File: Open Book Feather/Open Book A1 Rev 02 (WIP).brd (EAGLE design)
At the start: 77.5 x 112.3 mm, 124 parts, among them J1 SJ-43514-SMT, J2 10118193-0001LF, Q1 DMG341, Q2 IRLML0100, SW1 SPDT_SWITCH, U1 AP2112-3.3, U2 MCP73831T-2ACI/OT, U3 ATSAMD51J64-TQFP(10X10), U4 GD25Q16C (or GD25Q32C), U5 74AC165D, U6 GD25Q16C (or GD25Q32C), U7 23K256-I/SN, U8 MAX4466EXK+T, X1 JSTPH, X2 2x5 0.05" SWD

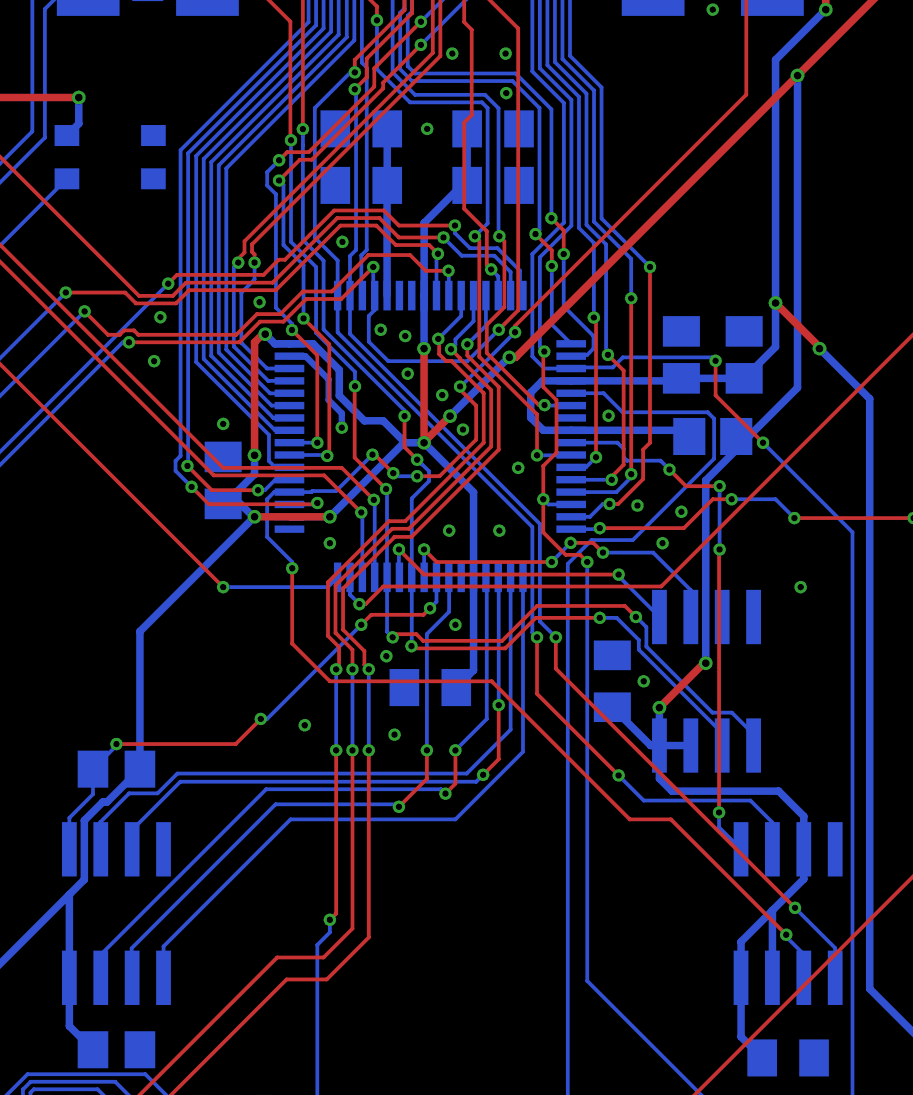
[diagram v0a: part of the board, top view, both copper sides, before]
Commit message: tweak documentation of QSPI flash
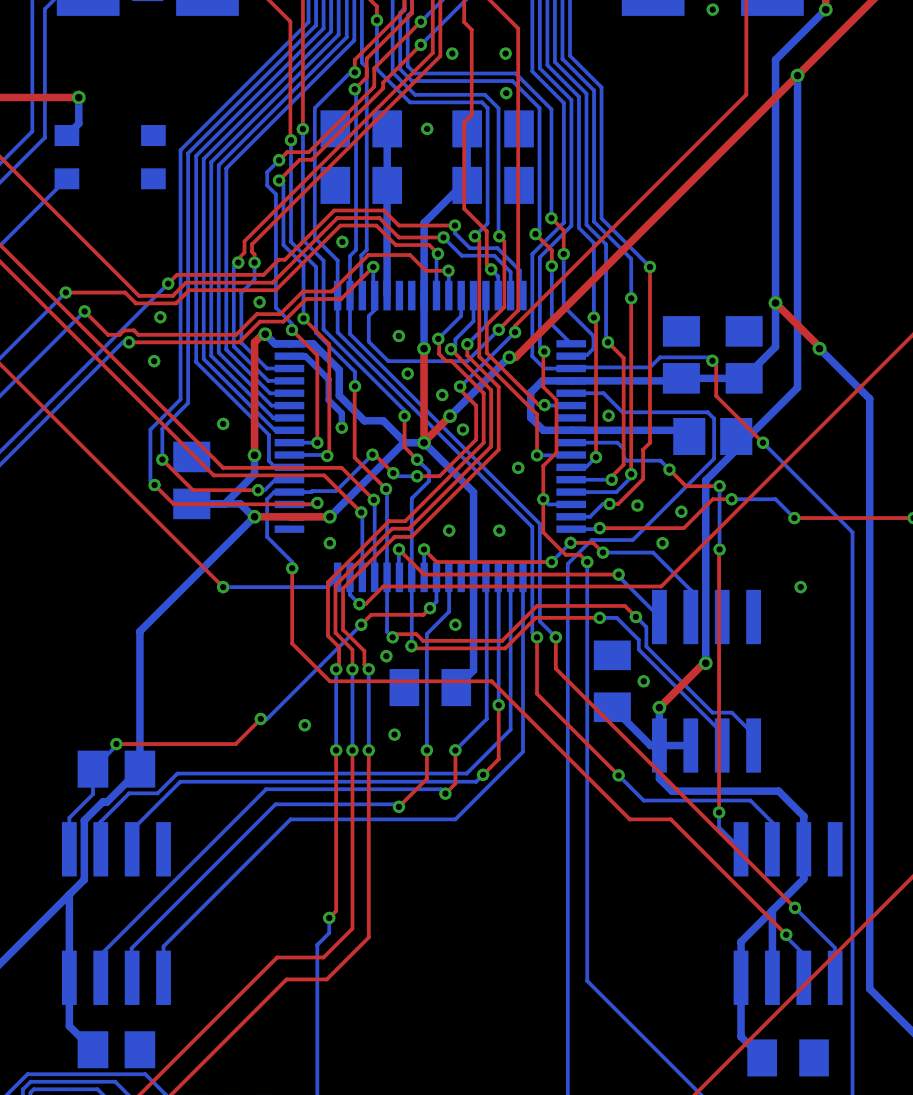
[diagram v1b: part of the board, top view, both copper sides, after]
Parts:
- moved C7 1.27 mm to (29.2, 48.3)
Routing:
- net +3V3: track 531.7 -> 534.3 mm
- net D5: track 41.3 -> 43.0 mm
- net D6: track 41.0 -> 42.3 mm
- net GND: vias 50 -> 49
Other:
- board text added: "U4 is another GD25Q16C Flash chip. It's the CIRCUITPY drive that shows up when you plug it in! It's on a dedicated QSPI bus (D35-D40/PA08-PA11, PB10, PB11). R9 pulls U4's CS high; the microcontroller can drive it low (active) via QSPI_CS (D36)."
- board text removed: "U4 is another GD25Q16C Flash chip on a dedicated QSPI bus (D35-D40/PA08-PA11 & PB10- PB11). It's the CIRCUITPY drive that shows up when you plug it in! R9 pulls U4's CS high; the microcontroller can drive it low (active) via QSPI_CS (D36)."

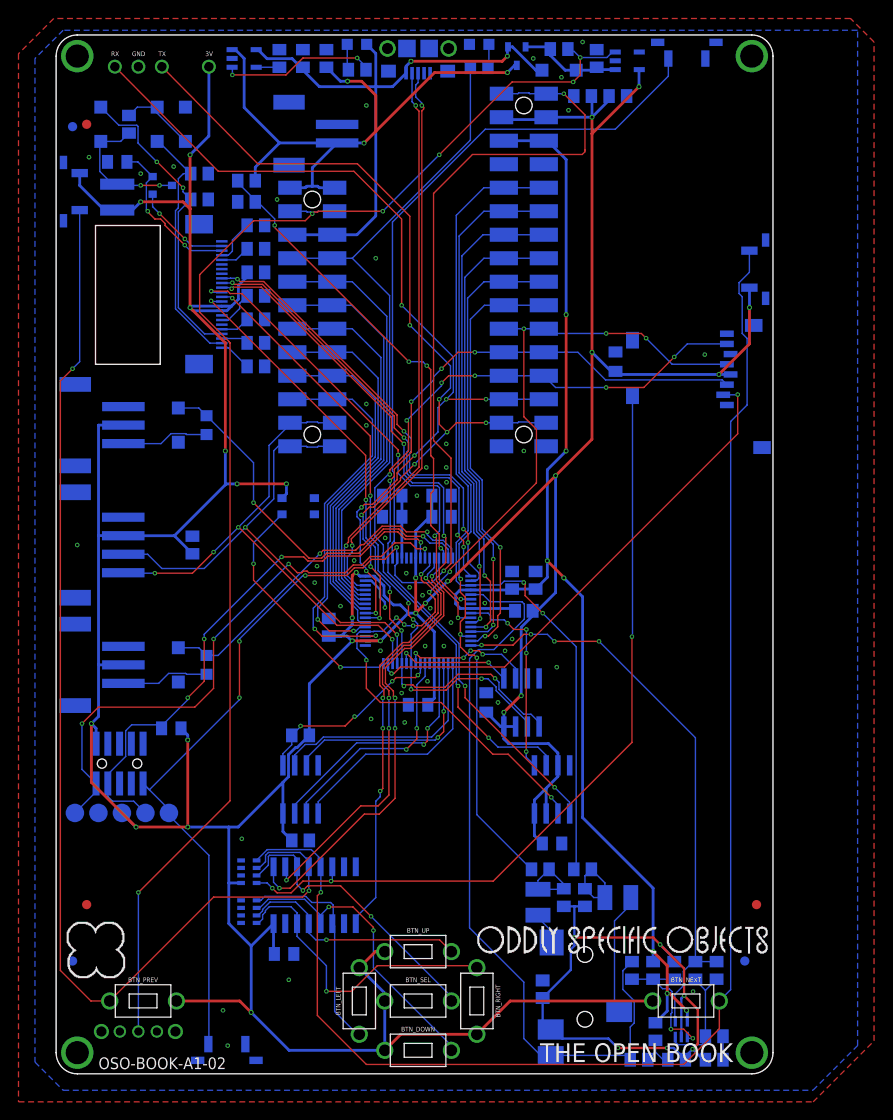
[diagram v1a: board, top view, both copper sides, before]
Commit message: more silkscreen tweaks
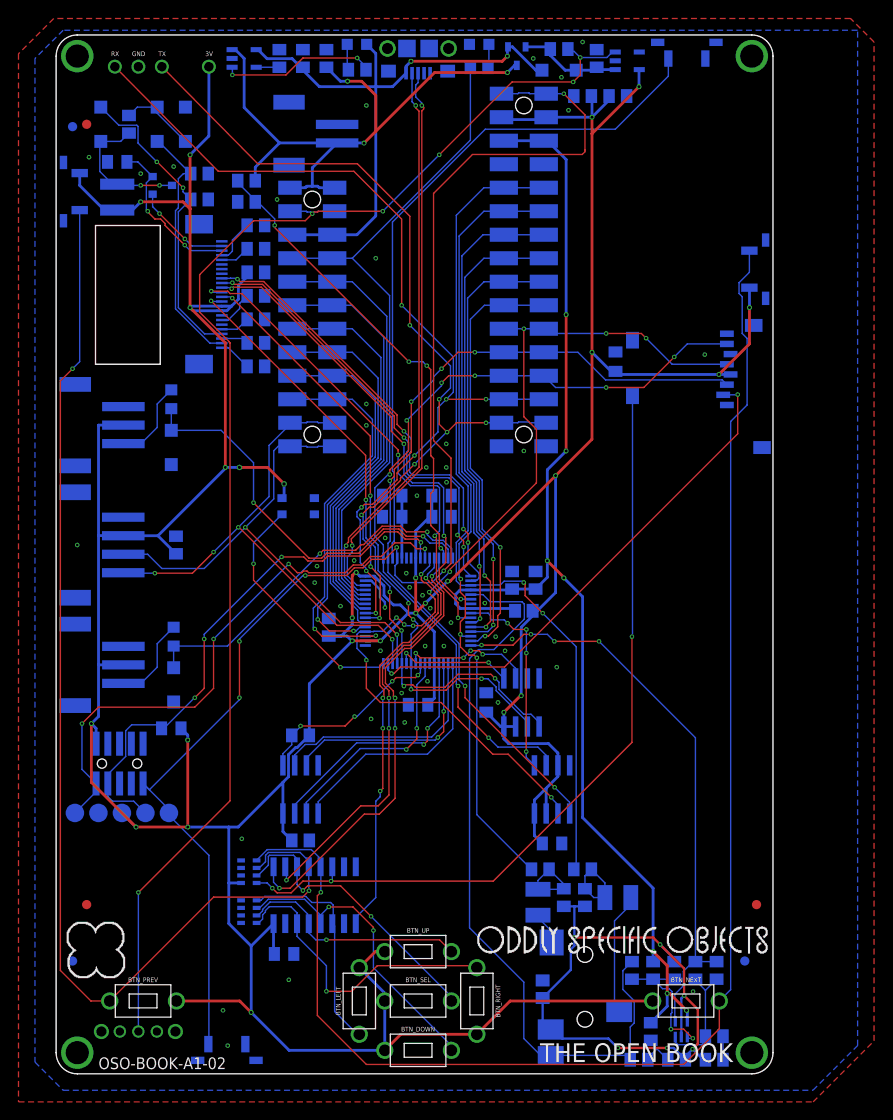
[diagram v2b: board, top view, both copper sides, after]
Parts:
- moved R18 4.72 mm to (12.2, 72.9), turned to 270 degrees
- moved R17 4.68 mm to (12.4, 47.2), turned to 270 degrees
- moved D6 2.53 mm to (12.2, 67.7)
- moved D5 2.22 mm to (12.4, 42.0)
- moved C27 1.78 mm to (12.7, 57.1)
- moved R23 0.51 mm to (64.0, 4.57)
- moved U$45 0.13 mm to (38.5, 94.2)
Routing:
- net D3_A9: track 41.6 -> 43.7 mm
- net D2_A8: track 37.9 -> 40.0 mm
- net N$65: track 4.12 -> 4.96 mm
- net +3V3: track 534.3 -> 533.6 mm
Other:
- board text added: "A8"
- board text added: "A9"
- board text added: "The Open Book by Joey Castillo @josecastillo. Based in large part on @Adafruit's awesome open source designs! OSO logo & lazer bear by Joseph Devens, @DoctorDevens. Thanks to Tom F, Josh L, Brent R & many others. Made with . in Brooklyn & Texas."
- board text added: "The center port provides an I²C interface. The other two ports provide access to pins A8 and A9 (PB03 & PB02, respectively) via current limiting resistors R17 & R18. D5 & D6 are 3.6V zener diodes to protect pins from overvoltage: they shunt excess power to ground when voltage exceeds their breakdown point."
- board text removed: "A1"
- board text removed: "A2"
- board text removed: "The Open Book by Joey Castillo @josecastillo. Based in large part on @Adafruit's great open source designs. OSO logo & lazer bear by Joseph Devens, @DoctorDevens. Thanks to Tom F, Josh L, Brent R & many others. Made with . in Brooklyn & Texas."
- board text removed: "The center port provides an I2C interface. The other two ports provide access to pins A8 and A9. D5 & D6 + R17 & R18 provide protection and current limiting."

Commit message: renumber passives, update silkscreen
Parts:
- removed C35: 10uF, microbuilder:0805-NO
- removed R26, R27: 100K, resistor array:EXBV8V
- added C13: 1uF, microbuilder:0805-NO
- added R6: 270, microbuilder:0805-NO
- added R7: 100K, microbuilder:0805-NO
- C17: value 1uF -> 1uF/25V
- C23: value 1uF/25V -> 4.7uF/25V
- C24: value 4.7uF/25V -> 10uF; device microbuilder:0805-NO -> microbuilder:0805_10MGAP
- C25: value 10uF -> 1uF
- C26: value 1uF -> 10uF; device microbuilder:0805_10MGAP -> microbuilder:0805-NO
- C27: value 10uF -> 1uF; device microbuilder:0805-NO -> microbuilder:0805_10MGAP
- C29: value 1uF -> 100uF; device microbuilder:0805_10MGAP -> resistor:C1210
- C31: value 100uF -> 0.1µF; device resistor:C1210 -> microbuilder:0805-NO
- C32: value 0.1µF -> 0.01uF
- C33: value 0.01uF -> 100pF
- C34: value 100pF -> 10uF
- R10: value 1M -> 0.47ohm; device microbuilder:0805-NO -> microbuilder:0805_10MGAP
- R11: value 1M -> 100K; device microbuilder:0805-NO -> resistor array:EXBV8V
- R12: device microbuilder:0805-NO -> resistor array:EXBV8V
- R13: device microbuilder:0805-NO -> microbuilder:_0805MP
- R14: value 100K -> 1K; device microbuilder:0805-NO -> microbuilder:_0805MP
- R15: value 100K -> 100
- R16: value 0.47ohm -> 100; device microbuilder:0805_10MGAP -> microbuilder:0805-NO
- R17, R18: value 1K -> 100; device microbuilder:_0805MP -> microbuilder:0805-NO
- R19, R20: value 100 -> 1K
- R21, R22: value 100 -> 1M
- R24: value 1K -> 100K
- R8: value 270 -> 100K
- moved R10 106.1 mm to (6.35, 98.6), turned to 0 degrees
- moved R16 94.2 mm to (56.9, 19.1), turned to 90 degrees
- moved R15 82.8 mm to (56.6, 22.1)
- moved C25 73.3 mm to (24.4, 13.0), turned to 180 degrees
- moved R18 68.5 mm to (54.6, 19.1), turned to 90 degrees
- moved R13 68.0 mm to (12.4, 47.2), turned to 270 degrees
- moved C14 66.6 mm to (21.3, 91.7), turned to 0 degrees
- moved C24 58.5 mm to (60.2, 77.0)
- moved R9 58.0 mm to (20.3, 94.2)
- moved C27 51.9 mm to (53.3, 24.9), turned to 180 degrees
- moved R12 48.7 mm to (20.6, 17.5), turned to 0 degrees
- moved R17 46.9 mm to (52.1, 22.1), turned to 0 degrees
- moved C26 45.7 mm to (12.7, 57.1), turned to 90 degrees
- moved R11 45.0 mm to (20.6, 21.8), turned to 0 degrees
- moved R8 28.0 mm to (20.3, 96.5), turned to 0 degrees
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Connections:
- net +3V3: now also C13.1, C16.2, C24.1, R11.5, R7.1; no longer C14.1, C17.2, C29.1, R26.5, R9.1
- net A0: now also R15.2; no longer R19.2
- net A1: now also R17.2; no longer R21.2
- net A10_MICAMP: now also C33.1, R24.2; no longer C34.1, R12.2
- net A6_VMEAS: now also R8.2, R9.1; no longer R14.1, R15.2
- net A7_MIC: now also C32.1, R19.1; no longer C33.1, R13.1
- net A8_: now also R13.1; no longer R17.1
- net A9_: now also R14.1; no longer R18.1
- net AGND: now also C31.2, C34.2, R16.1, R18.1, R21.1; no longer C32.2, C35.2, R10.1, R20.1, R22.1
- net AUDIO_LEFT: now also C30.2; no longer C31.2
- net AUDIO_RIGHT: now also C29.2; no longer C30.2
- net AVCC: now also R20.2, R22.2; no longer R11.2, R23.2
- net BUTTON0: now also R12.1; no longer R27.1
- net BUTTON1: now also R12.2; no longer R27.2
- net BUTTON2: now also R12.3; no longer R27.3
- net BUTTON3: now also R12.4; no longer R27.4
- net BUTTON4: now also R11.3; no longer R26.3
- net BUTTON5: now also R11.2; no longer R26.2
- net BUTTON6: now also R11.1; no longer R26.1
- net BUTTON7: now also R11.4; no longer R26.4
- net D13: now also R6.1; no longer R8.1
- net D2_A8: now also R13.2; no longer R17.2
- net D3_A9: now also R14.2; no longer R18.2
- net GND: now also C13.2, C14.1, C21.2, C24.2, R10.2, R11.6, R11.7, R11.8, R12.5, R12.6, R12.7, R12.8, R9.2; no longer C14.2, C21.1, C23.2, C29.2, R14.2, R16.2, R26.6, R26.7, R26.8, R27.5, R27.6, R27.7, R27.8
- net N$15: now also C30.1, R17.1, R18.2; no longer C31.1, R21.1, R22.2
- net N$2: now also C23.2; no longer C24.2
- net N$3: now also C23.1; no longer C24.1
- net N$65: now also C31.1, R19.2, R20.1; no longer C32.1, R13.2, R23.1
- net N$67: now also C32.2, R21.2, R22.1; no longer C33.2, R10.2, R11.1
- net N$68: now also C33.2, R23.1; no longer C34.2, R12.1
- net N$69: now also C34.1, R23.2; no longer C35.1, R24.2
- net N$7: now also R6.2; no longer R8.2
- net N$70: now also C29.1, R15.1, R16.2; no longer C30.1, R19.1, R20.2
- net PREVGH: now also C22.1; no longer C23.1
- net PREVGL: now also C21.1; no longer C22.1
- net QSPI_CS: now also R7.2; no longer R9.2
- net RESE: now also R10.1; no longer R16.1
- net VBAT: now also R8.1; no longer R15.1
- net VCOM: now also C20.2; no longer C21.2
- net VDD: now also C17.2; no longer C18.2
- net VGH: now also C15.2; no longer C16.2
- net VGL: now also C14.2; no longer C15.2
- net VSH: now also C18.2; no longer C19.2
- net VSL: now also C19.2; no longer C20.2
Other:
- board text added: "BTN_RESET pulls !RESET low, resetting the MCU. Double-tap to enter UF2 bootloader."
- board text added: "C11 & C12 filter AVCC/ AREF, isolated by FB1"
- board text added: "D1&Q1 conspire to let only the higher of VBAT & VBUS reach 3.3V regulator U1. C1 filters regulator input; C2 & C3 filter output. R1 pulls EN high to keep the regulator on. BATTERY: U2 is a LiPo charging controller. Powered by VBUS, it charges the battery at a rate determined by R3. C4=filter for VBAT, R4 limits current to CHG LED. R8 & R9 are a voltage divider for VBAT to make a battery gauge on 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"
- board text added: "LOCKBUTTON=D51=PA27"
- board text added: "Pins: BUTTON_LATCH: D48/PB31 BUTTON_OUT: D49/PB30 BUTTON_CLOCK: D50/PB00"
- board text added: "R1 up top pulls EN high. Switching SW1 pulls EN low, disabling pwr supply U1 along with most of the board."
- board text added: "R11-R12 are resistor arrays to keep inputs from floating. C25 (& many small capacitors you see near devices) are bypass caps; they filter current spikes & dips."
- board text added: "The center port provides an I²C interface. The other two ports provide access to pins A8 and A9 (PB03 & PB02, respectively) via current limiting resistors R13 & R14. D5 & D6 are 3.6V zener diodes to protect pins from overvoltage: they shunt excess power to ground when the voltage exceeds their breakdown point."
- board text added: "U4 is another GD25Q16C Flash chip. It's the CIRCUITPY drive that shows up when you plug it in! It's on a dedicated QSPI bus (PB10, PB11, PA08-PA11). CircuitPy uses this internally; Arduino can use it with SCK 35, CS 36 and data lines 37-40."
- board text removed: "C11 & C12 filter AVCC, isolated via FB1."
- board text removed: "Clock: D48/PB31 Data: D49/PB30 Latch: D50/PB00"
- board text removed: "D1&Q1 conspire to let only the higher of VBAT & VBUS reach 3.3V regulator U1. C1 filters regulator input; C2 & C3 filter output. R1 pulls EN high to keep the regulator on. BATTERY: U2 is a LiPo charging controller. Powered by VBUS, it charges the battery at a rate determined by R3. C4=filter for VBAT, R4 limits current to CHG LED. R14 & R15: a voltage divider for VBAT to make a battery gauge on A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"
- board text removed: "R1 up top pulls EN high. Switching SW1 pulls EN low, disabling power supply U1 along with most of the board."
- board text removed: "R26-R27: pull-up & pull-down resistor arrays."
- board text removed: "R6 pulls reset high. BTN_RESET pulls it low. Double-tap to enter UF2 bootloader."
- board text removed: "The center port provides an I²C interface. The other two ports provide access to pins A8 and A9 (PB03 & PB02, respectively) via current limiting resistors R17 & R18. D5 & D6 are 3.6V zener diodes to protect pins from overvoltage: they shunt excess power to ground when voltage exceeds their breakdown point."
- board text removed: "U4 is another GD25Q16C Flash chip. It's the CIRCUITPY drive that shows up when you plug it in! It's on a dedicated QSPI bus (D35-D40/PA08-PA11, PB10, PB11). R9 pulls U4's CS high; the microcontroller can drive it low (active) via QSPI_CS (D36)."
